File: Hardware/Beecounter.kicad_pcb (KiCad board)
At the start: 2 copper layers, 171 parts, among them J1 Conn_01x03, J10 Conn_01x03, J11 Conn_01x03, J12 Conn_01x03, J13 Conn_01x03, J14 Conn_01x03, J15 Conn_02x20_Odd_Even, J16 Conn_01x04, J17 Conn_01x10, J2 Conn_01x03, J3 Conn_01x03, J4 Conn_01x03, J5 Conn_01x03, J6 Conn_01x03, J7 Conn_01x03, J8 Conn_01x03, J9 Conn_01x03, U1 LM393, U10 LM393, U11 H2010, U12 LM393, U13 H2010, U14 LM393, U15 H2010, U16 LM393, U17 H2010, U18 LM393, U19 H2010, U2 H2010, U20 LM393, U21 H2010, U22 LM393, U23 H2010, U24 LM393, U25 H2010, U26 LM393, U27 H2010, U28 LM393, U3 H2010, U4 LM393, U5 H2010, U6 LM393, U7 H2010, U8 LM393, U9 H2010

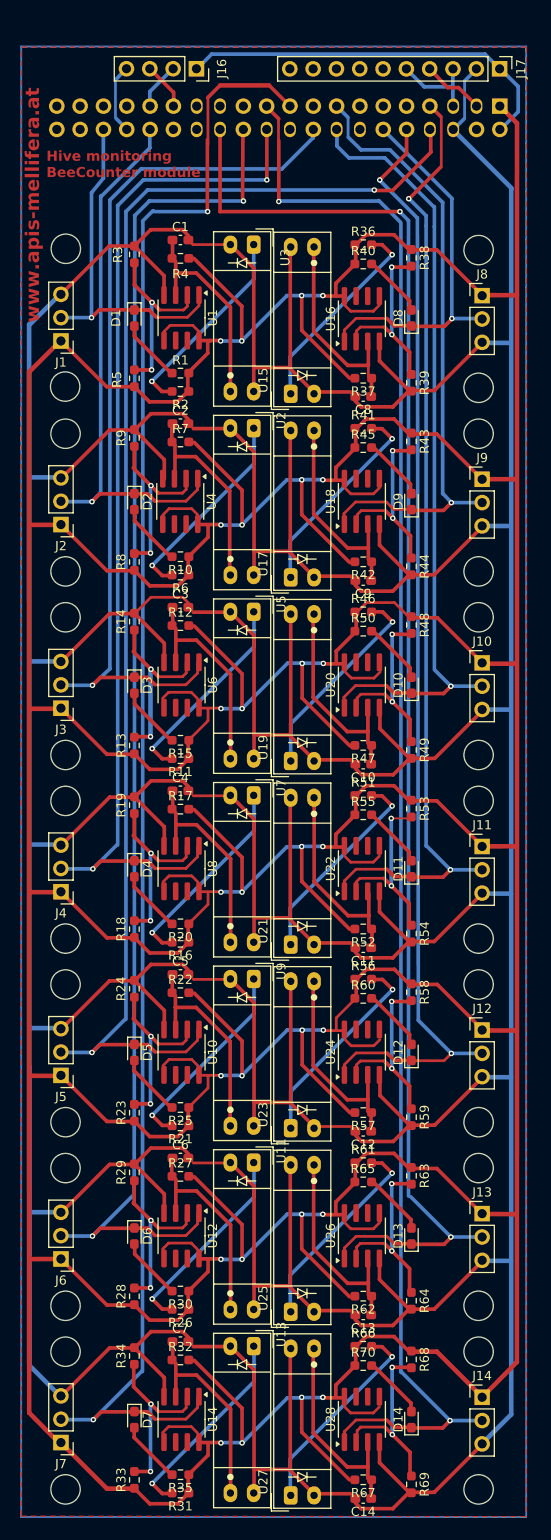
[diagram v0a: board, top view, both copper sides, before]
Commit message: Completed BeeCounter v1.1 from milling/drilling
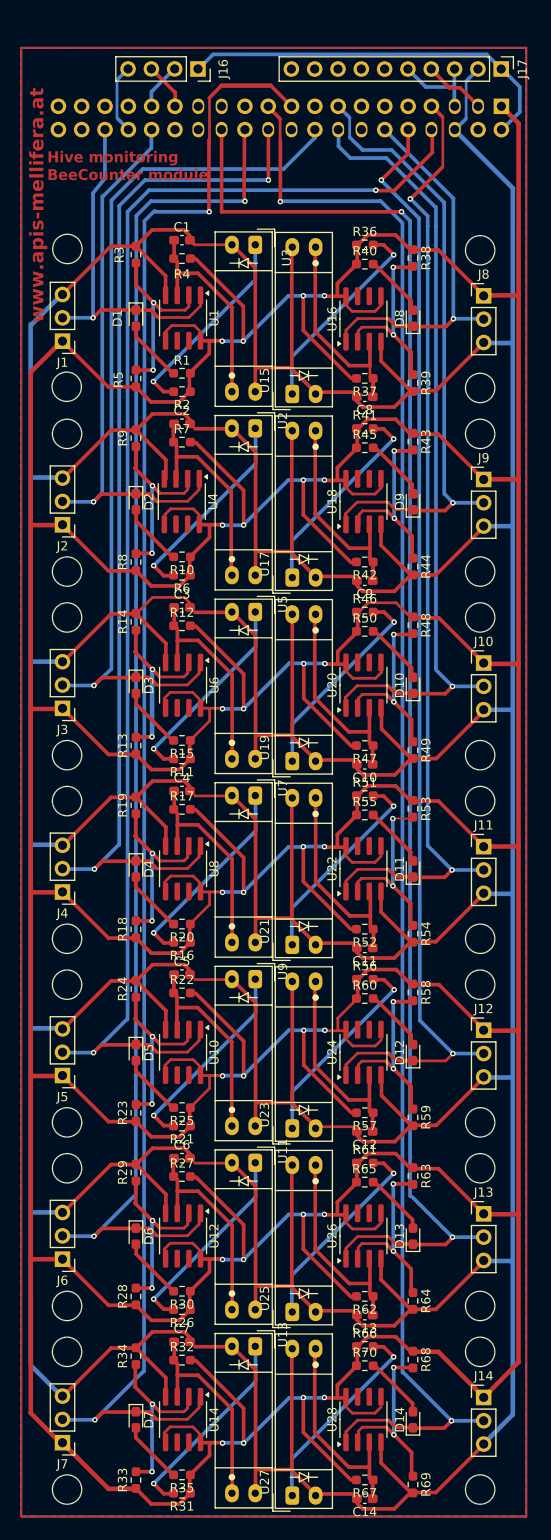
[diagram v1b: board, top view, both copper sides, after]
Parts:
- moved ? 0.17 mm to (90.0, 97.1)
- moved ? 0.17 mm to (90.0, 197.1)
- moved ? 0.17 mm to (90.0, 157.1)
- moved ? 0.17 mm to (90.0, 162.1)
- moved ? 0.17 mm to (90.0, 142.1)
- moved ? 0.17 mm to (90.0, 102.1)
- moved ? 0.17 mm to (90.0, 82.1)
- moved ? 0.17 mm to (90.0, 122.1)
- moved ? 0.17 mm to (90.0, 177.1)
- moved ? 0.17 mm to (90.0, 137.1)
- moved ? 0.17 mm to (90.0, 117.1)
- moved ? 0.17 mm to (90.0, 77.1)
- moved ? 0.17 mm to (90.0, 182.1)
- moved C10 0.17 mm to (77.4, 118.1)
- moved C11 0.17 mm to (77.4, 138.1)
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
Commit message: Red layer 0.5mm
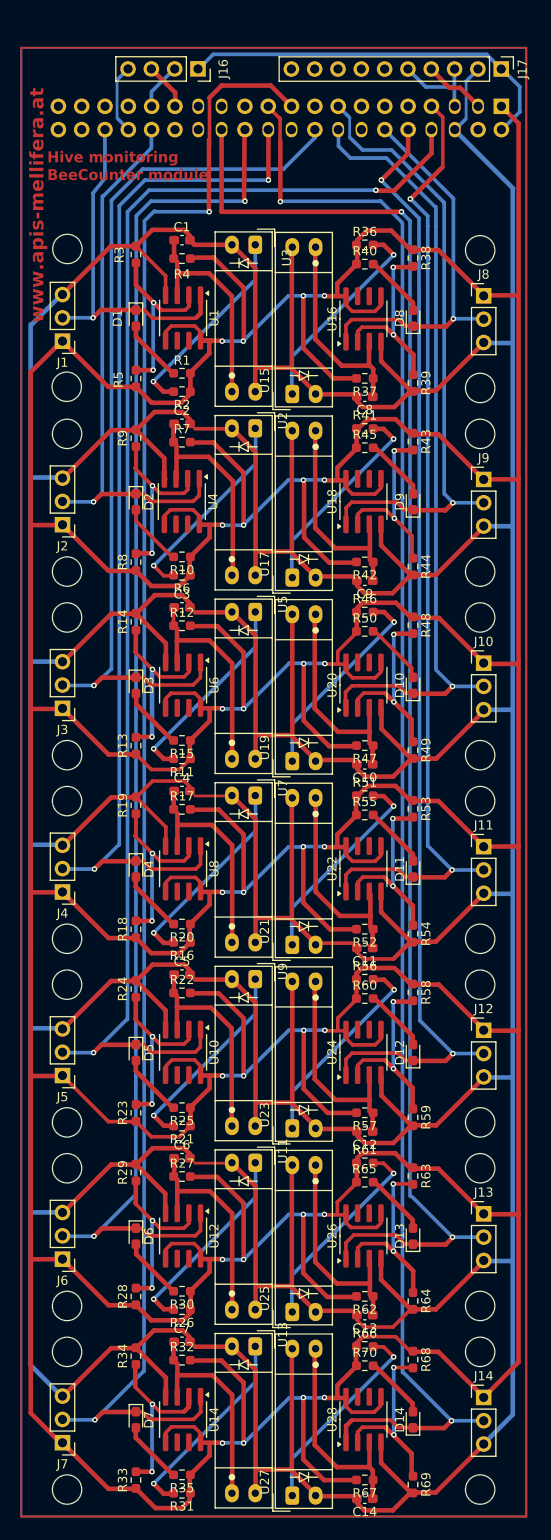
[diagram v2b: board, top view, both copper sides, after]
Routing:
- net +3.3V: track 673.8 -> 697.2 mm
- net GND: track 656.8 -> 660.3 mm
- net Net-(U14A-+): track 22.8 -> 23.8 mm
- net Net-(U8A-+): track 22.8 -> 23.7 mm
- net Net-(U18A-+): track 22.8 -> 23.7 mm
- net Net-(U6A-+): track 22.8 -> 23.7 mm
- net Net-(U12A-+): track 22.9 -> 23.8 mm
- net Net-(U4A-+): track 22.8 -> 23.7 mm
- net Net-(U10A-+): track 22.8 -> 23.7 mm
- net Net-(U24A-+): track 22.8 -> 23.7 mm
- net Net-(U26A-+): track 22.8 -> 23.6 mm
- net Net-(D4-K): track 9.06 -> 9.80 mm
- net Net-(U22A-+): track 22.8 -> 23.5 mm
- net Net-(U1A-+): track 22.8 -> 23.5 mm
- net Net-(U20A-+): track 22.8 -> 23.5 mm
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- removed copper zone on B.Cu, net GND
- removed copper zone on F.Cu, net GND

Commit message: Corrected red layer
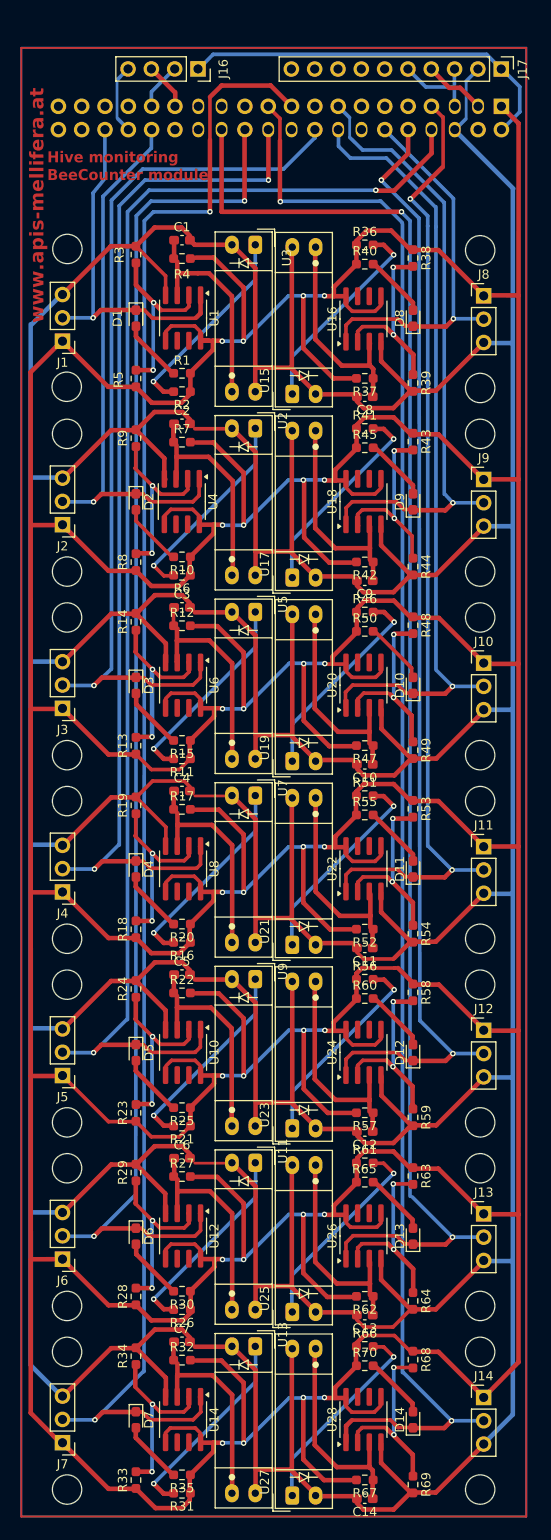
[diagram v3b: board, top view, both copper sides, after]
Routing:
- net +3.3V: track 697.2 -> 700.9 mm
- net GND: track 660.3 -> 661.5 mm

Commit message: Final version 1.1
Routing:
- net Net-(D12-K): track 9.46 -> 10.7 mm
- net Net-(D11-K): track 9.45 -> 10.2 mm
- added copper zone on B.Cu, net GND
- added copper zone on F.Cu, net GND
